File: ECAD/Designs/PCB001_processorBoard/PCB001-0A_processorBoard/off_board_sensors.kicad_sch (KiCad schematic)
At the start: 5 parts

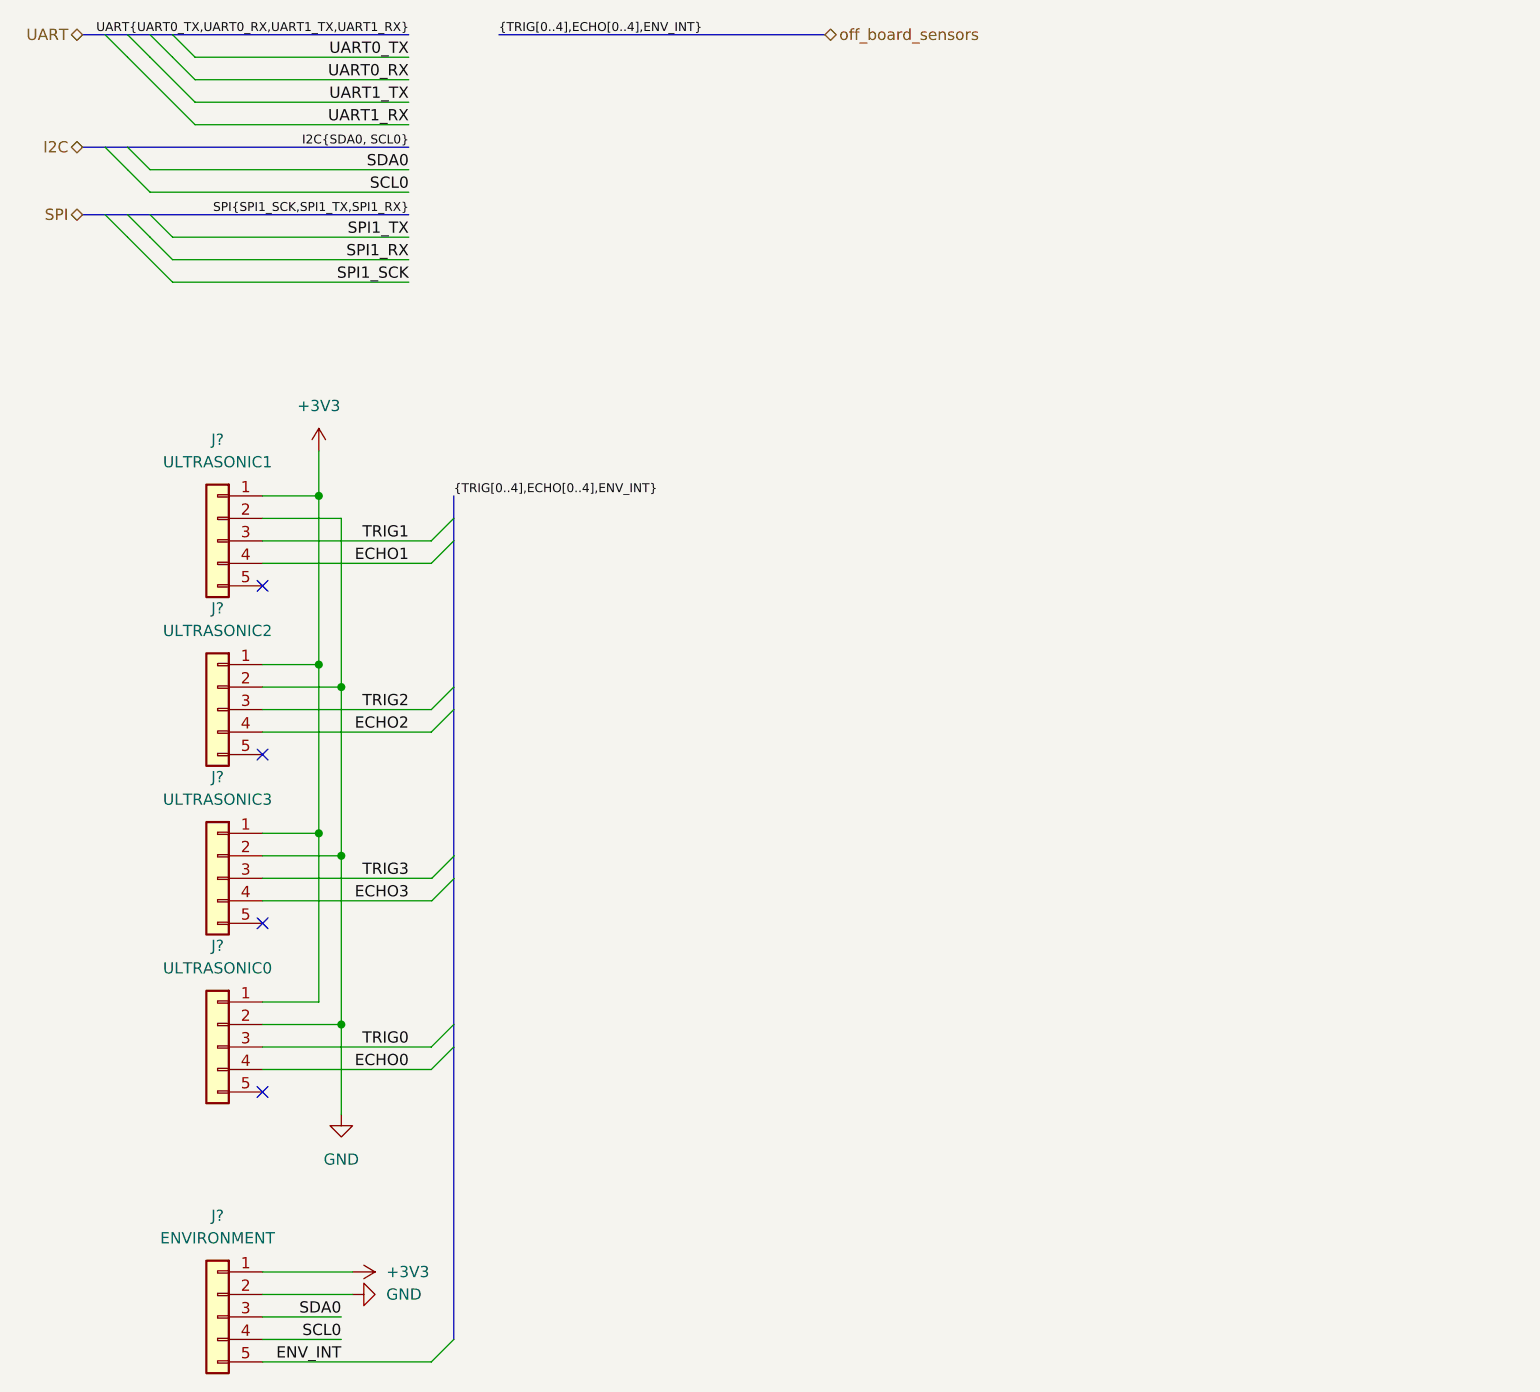
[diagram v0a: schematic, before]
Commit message: added more connectors to the side of the PCB, added a basic power supply, and began putting parts on the PCB.
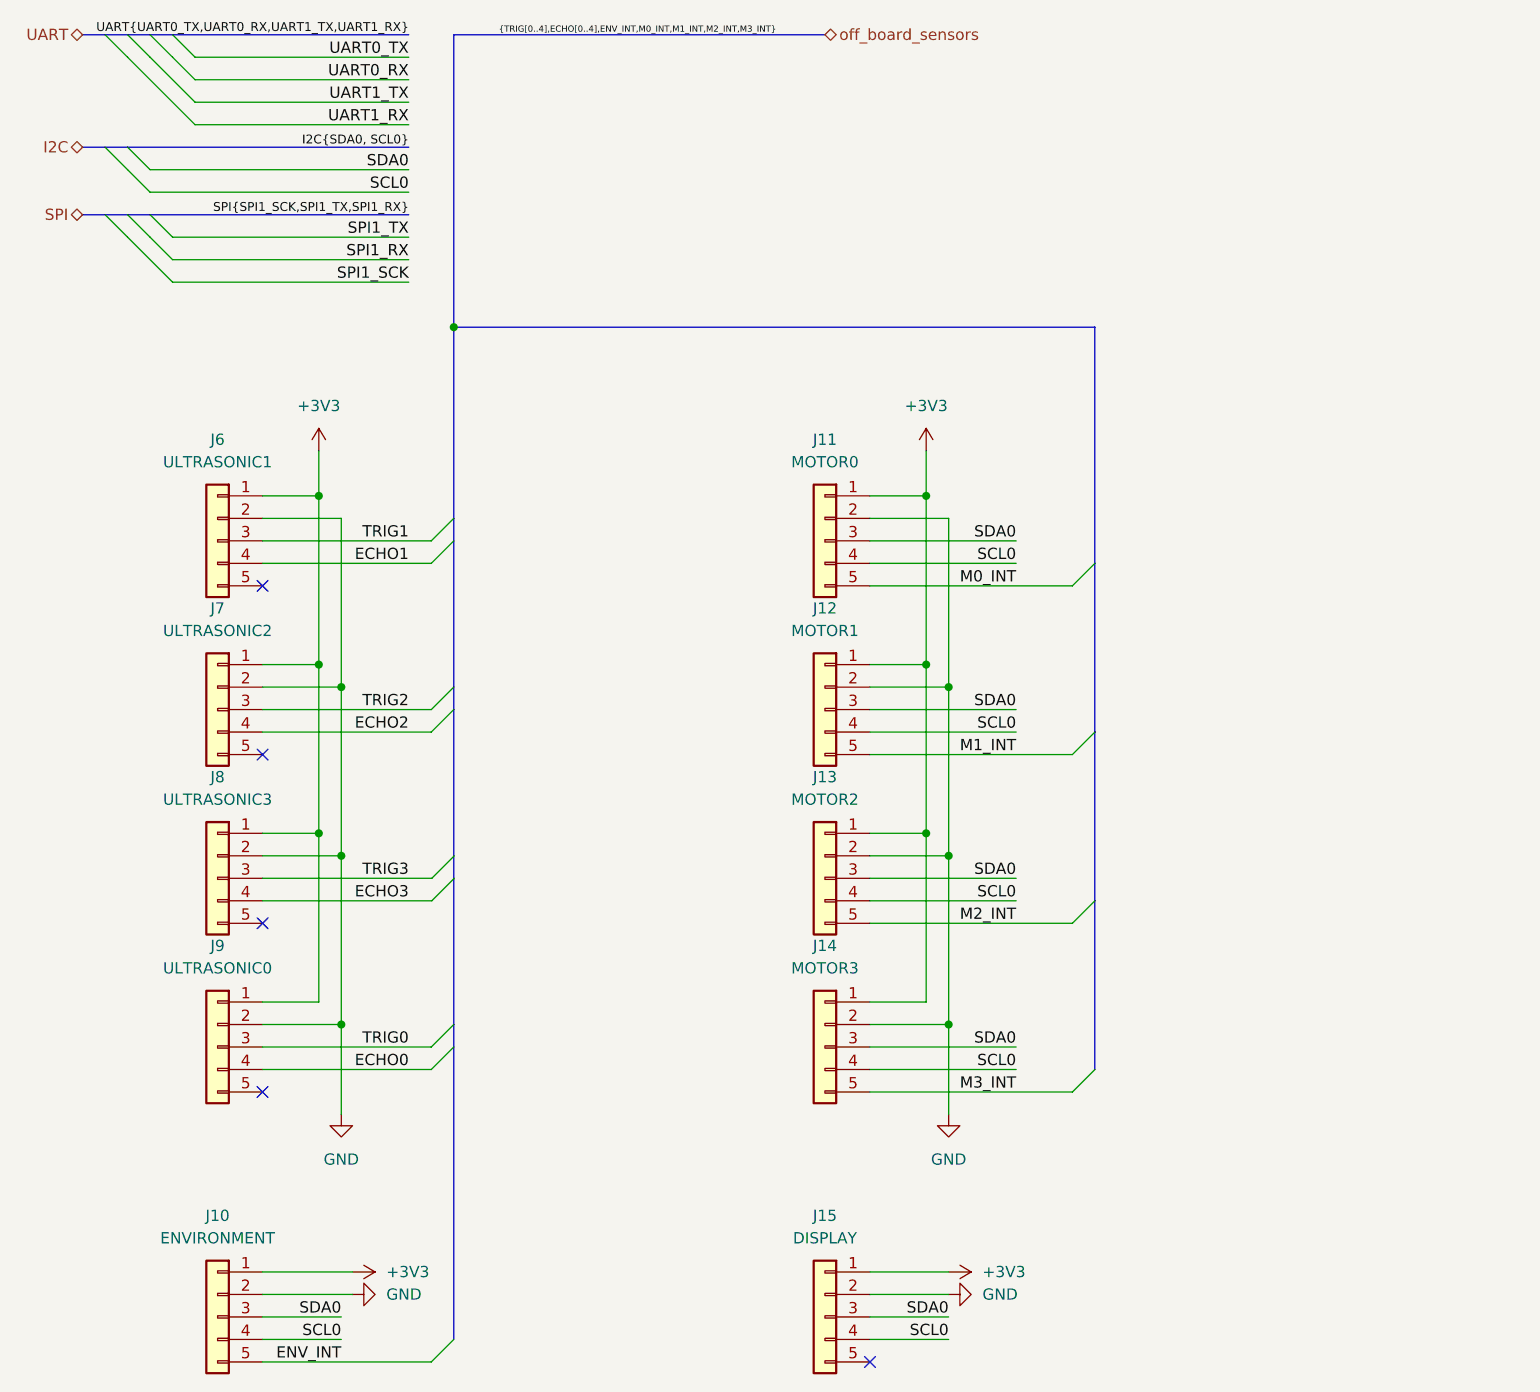
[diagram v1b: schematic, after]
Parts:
- added J11: MOTOR0, Connector_Molex:Molex_PicoBlade_53047-0510_1x05_P1.25mm_Vertical, symbol Connector_Generic:Conn_01x05
- added J12: MOTOR1, Connector_Molex:Molex_PicoBlade_53047-0510_1x05_P1.25mm_Vertical, symbol Connector_Generic:Conn_01x05
- added J13: MOTOR2, Connector_Molex:Molex_PicoBlade_53047-0510_1x05_P1.25mm_Vertical, symbol Connector_Generic:Conn_01x05
- added J14: MOTOR3, Connector_Molex:Molex_PicoBlade_53047-0510_1x05_P1.25mm_Vertical, symbol Connector_Generic:Conn_01x05
- added J15: DISPLAY, Connector_Molex:Molex_PicoBlade_53047-0510_1x05_P1.25mm_Vertical, symbol Connector_Generic:Conn_01x05
- gave numbers to parts that had none: 5
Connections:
- net +3V3: now also J11.1 (Pin_1), J12.1 (Pin_1), J13.1 (Pin_1), J14.1 (Pin_1), J15.1 (Pin_1)
- net GND: now also J11.2 (Pin_2), J12.2 (Pin_2), J13.2 (Pin_2), J14.2 (Pin_2), J15.2 (Pin_2)
- net SCL0: now also J11.4 (Pin_4), J12.4 (Pin_4), J13.4 (Pin_4), J14.4 (Pin_4), J15.4 (Pin_4)
- net SDA0: now also J11.3 (Pin_3), J12.3 (Pin_3), J13.3 (Pin_3), J14.3 (Pin_3), J15.3 (Pin_3)
- new net M0_INT: J11.5 (Pin_5)
- new net M1_INT: J12.5 (Pin_5)
- new net M2_INT: J13.5 (Pin_5)
- new net M3_INT: J14.5 (Pin_5)
- no-connect marks 4 -> 5

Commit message: updated schematics
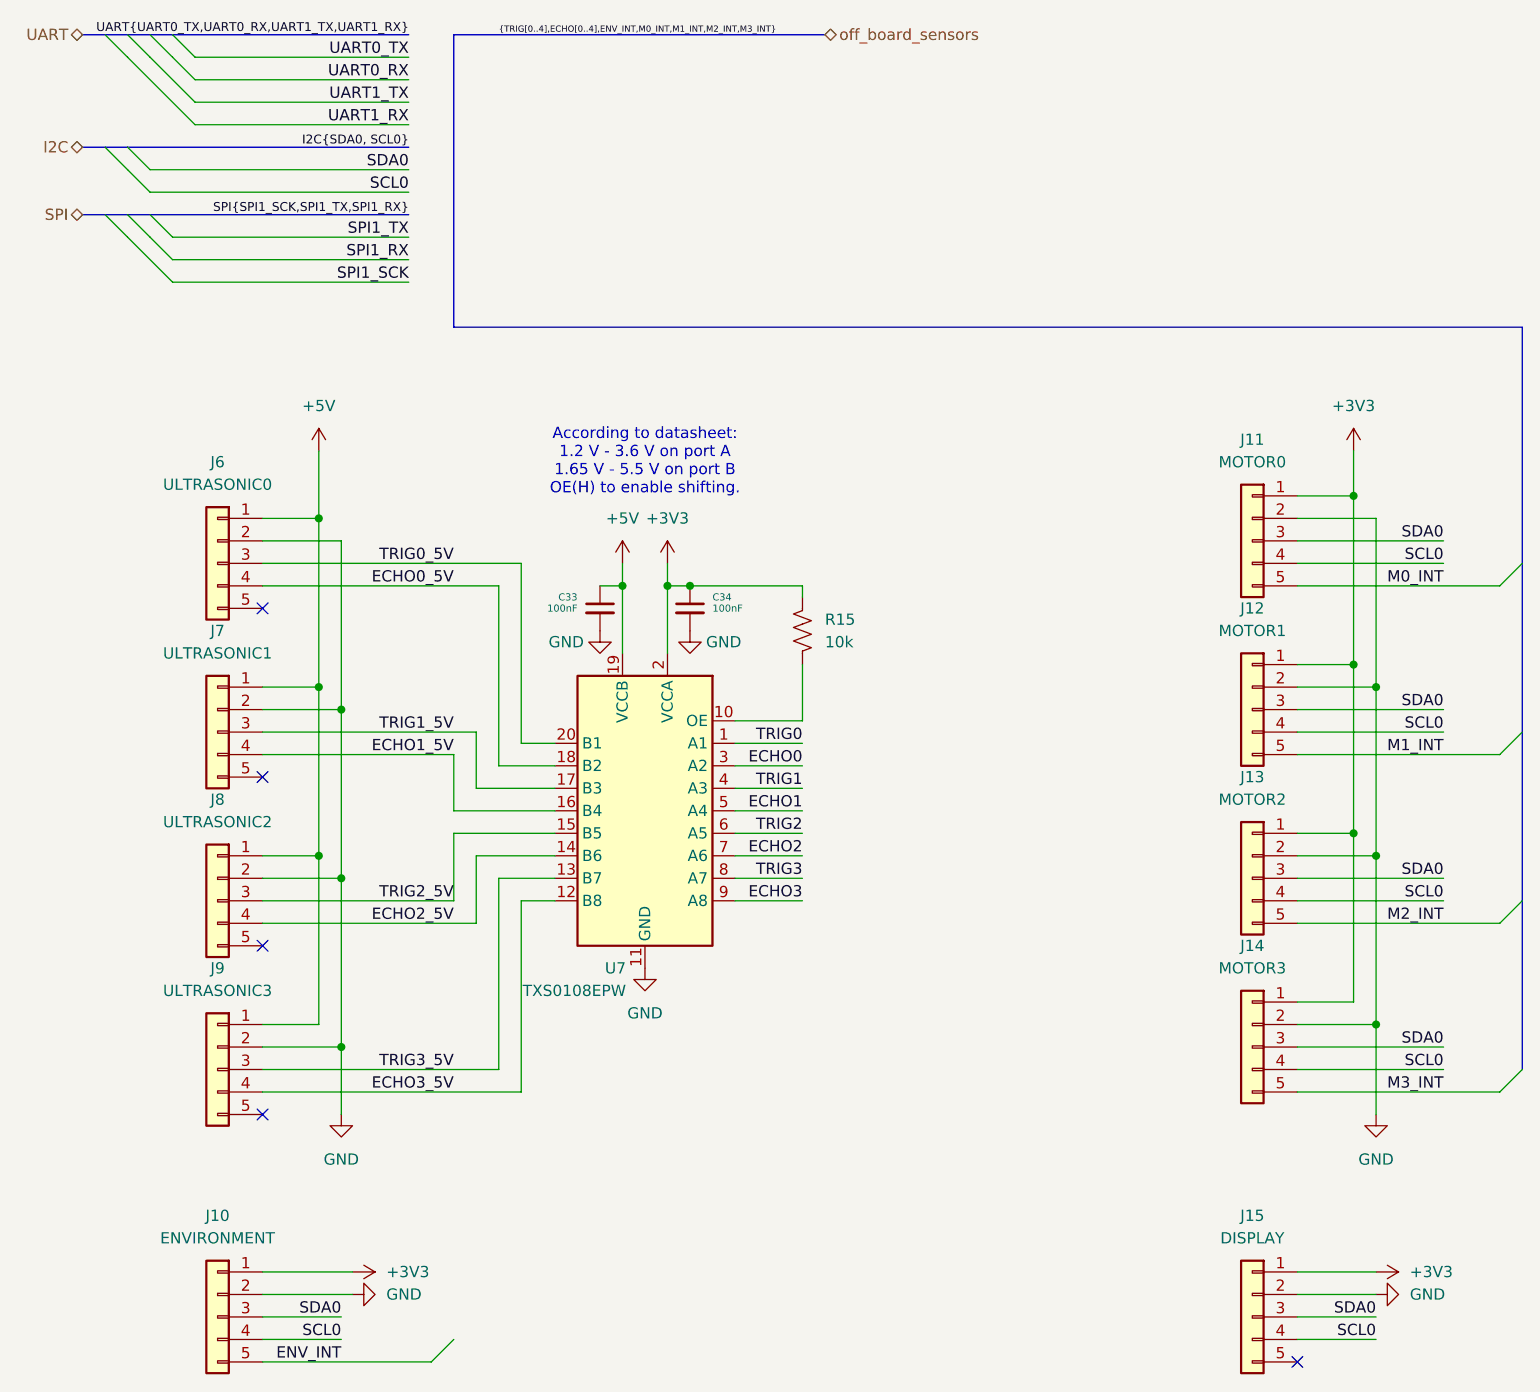
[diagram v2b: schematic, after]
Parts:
- added C33, C34: 100nF, Capacitor_SMD:C_0402_1005Metric_Pad0.74x0.62mm_HandSolder, symbol Device:C_Small
- added R15: 10k, Resistor_SMD:R_0402_1005Metric_Pad0.72x0.64mm_HandSolder, symbol Device:R_US
- added U7: TXS0108EPW, Package_SO:TSSOP-20_4.4x6.5mm_P0.65mm, symbol Logic_LevelTranslator:TXS0108EPW
- renumbered J9 to J6, J6 to J7, J7 to J8, J8 to J9
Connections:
- net +3V3: now also C34.1, R15.1, U7.2 (VCCA); no longer J6.1 (Pin_1), J7.1 (Pin_1), J8.1 (Pin_1), J9.1 (Pin_1)
- net ECHO0: now also U7.3 (A2); no longer J6.4 (Pin_4)
- net ECHO1: now also U7.5 (A4); no longer J7.4 (Pin_4)
- net ECHO2: now also U7.7 (A6); no longer J8.4 (Pin_4)
- net ECHO3: now also U7.9 (A8); no longer J9.4 (Pin_4)
- net GND: now also C33.2, C34.2, U7.11 (GND)
- net TRIG0: now also U7.1 (A1); no longer J6.3 (Pin_3)
- net TRIG1: now also U7.4 (A3); no longer J7.3 (Pin_3)
- net TRIG2: now also U7.6 (A5); no longer J8.3 (Pin_3)
- net TRIG3: now also U7.8 (A7); no longer J9.3 (Pin_3)
- new net: R15.2, U7.10 (OE)
- new net +5V: C33.1, J6.1 (Pin_1), J7.1 (Pin_1), J8.1 (Pin_1), J9.1 (Pin_1), U7.19 (VCCB)
- new net ECHO0_5V: J6.4 (Pin_4), U7.18 (B2)
- new net ECHO1_5V: J7.4 (Pin_4), U7.16 (B4)
- new net ECHO2_5V: J8.4 (Pin_4), U7.14 (B6)
- new net ECHO3_5V: J9.4 (Pin_4), U7.12 (B8)
- new net TRIG0_5V: J6.3 (Pin_3), U7.20 (B1)
- new net TRIG1_5V: J7.3 (Pin_3), U7.17 (B3)
- new net TRIG2_5V: J8.3 (Pin_3), U7.15 (B5)
- new net TRIG3_5V: J9.3 (Pin_3), U7.13 (B7)
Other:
- note added: "According to datasheet: 1.2 V - 3.6 V on port A 1.65 V - 5.5 V on port B OE(H) to enable shifting."
- moved on the sheet: J11, J12, J13, J14, J15, J6, J7, J8, J9
